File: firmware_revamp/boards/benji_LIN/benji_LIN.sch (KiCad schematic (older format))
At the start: 41 parts, among them J1 CONN_02X03, U1 MCP2561-E_SN, U101 TPS560430YF, U2 ATMEGA16M1, U3 TLIN1021DRQ1, Y1 Crystal_SMD

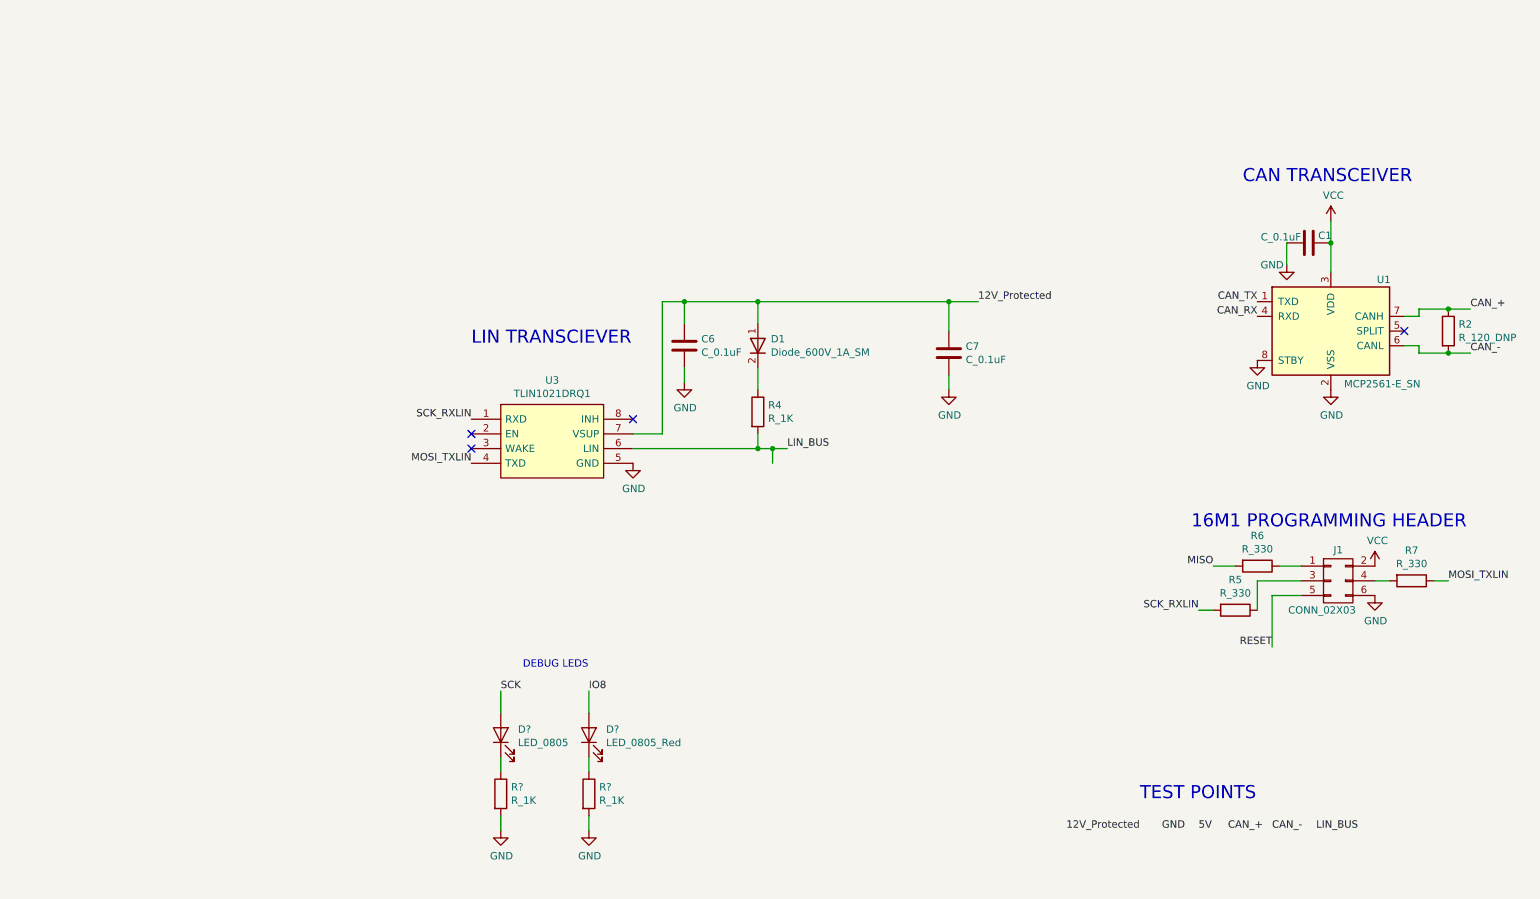
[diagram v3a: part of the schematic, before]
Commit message: Added blank headers, fixed programming resistors
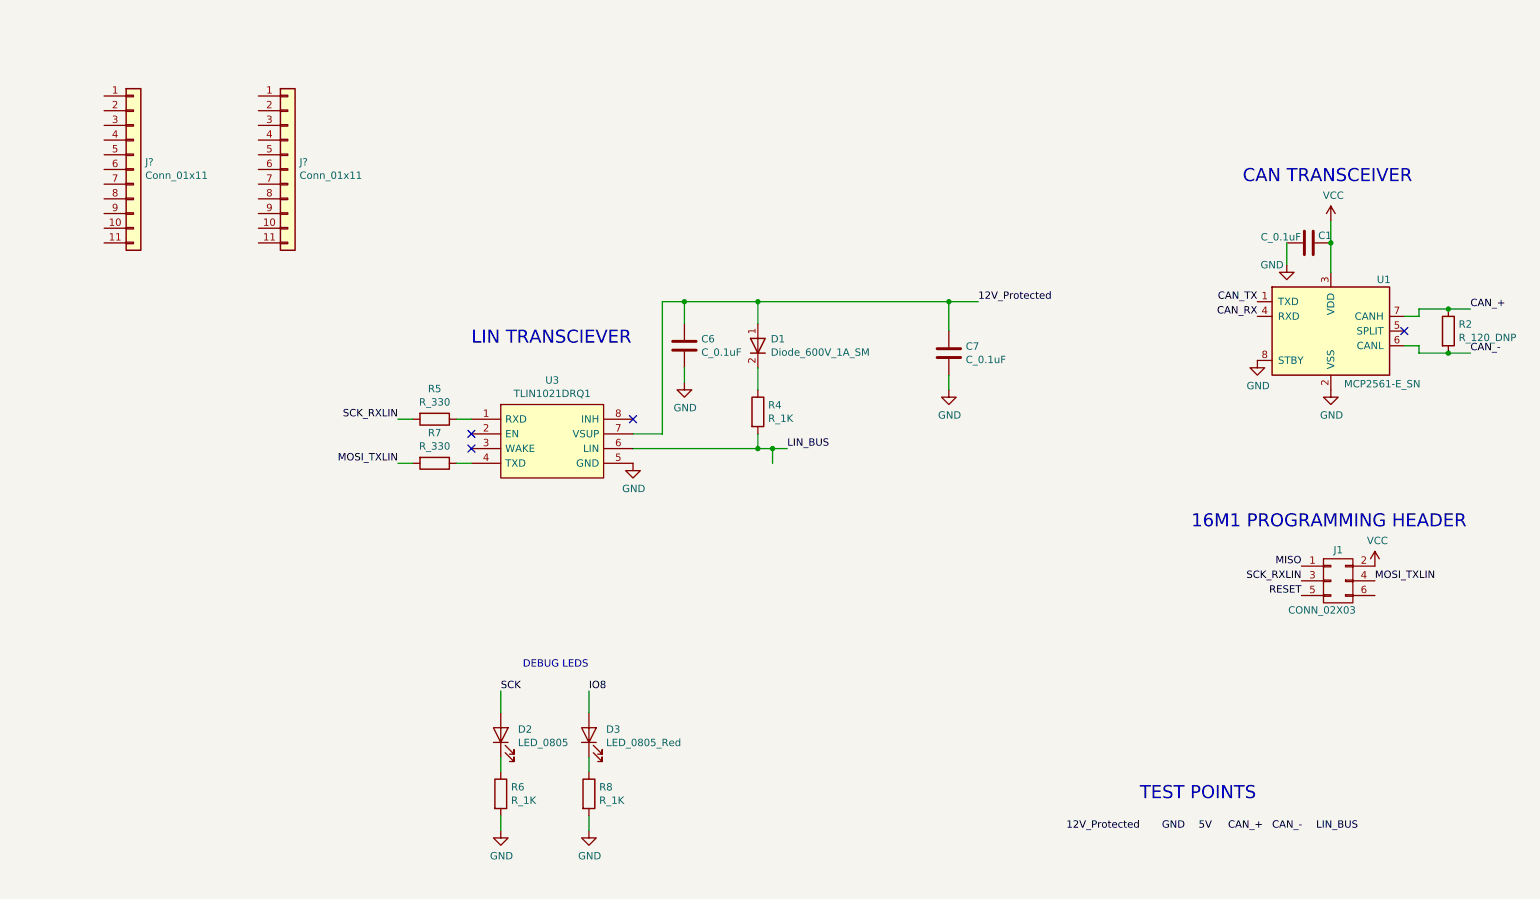
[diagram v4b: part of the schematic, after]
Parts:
- removed R6: R_330, footprints:R_0805_OEM, symbol formula:R_330
- added J? (x2): Conn_01x11, footprints:PinHeader_1x11_P2.54mm_Vertical, symbol formula:Conn_01x11
- gave numbers to parts that had none: 4
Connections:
- net GND: no longer J1.6 (P6)
- net MISO: now also J1.1 (P1)
- net MOSI_TXLIN: now also J1.4 (P4), R7.2; no longer R7.1, U3.4 (TXD)
- net SCK_RXLIN: now also J1.3 (P3); no longer U3.1 (RXD)
- net at R5.1: now also U3.1 (RXD); no longer J1.3 (P3)
- new net: R7.1, U3.4 (TXD)
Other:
- moved on the sheet: R7
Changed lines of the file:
@@
 Text Label 13300 7500 2    50   ~ 0
 GND
-Text Label 14600 4500 0    50   ~ 0
+Text Label 14100 4500 0    50   ~ 0
 MOSI_TXLIN
-$Comp
-L power:GND #PWR09
-U 1 1 5D62962D
-P 14100 4600
-F 0 "#PWR09" H 14100 4350 50  0001 C CNN
-F 1 "GND" H 14105 4427 50  0000 C CNN
-F 2 "" H 14100 4600 50  0001 C CNN
-F 3 "" H 14100 4600 50  0001 C CNN
-	1    14100 4600
-	1    0    0    -1
-$EndComp
 $Comp
 L power:VCC #PWR07
@@
 Text Label 3650 3100 0    50   ~ 0
 MOSI_TXLIN
-Text Label 7950 3400 2    50   ~ 0
+Text Label 7450 3400 2    50   ~ 0
 SCK_RXLIN
-Text Label 7950 3700 2    50   ~ 0
+Text Label 7450 3700 2    50   ~ 0
 MOSI_TXLIN
 $Comp
@@
 Wire Wire Line
 	2250 7350 2600 7350
-Text Label 12900 4700 2    50   ~ 0
+Text Label 13600 4500 2    50   ~ 0
 SCK_RXLIN
 $Comp
@@
 	1    0    0    -1
 $EndComp
-Text Label 13000 4400 2    50   ~ 0
+Text Label 13600 4400 2    50   ~ 0
 MISO
-Text Label 13400 4950 2    50   ~ 0
+Text Label 13600 4600 2    50   ~ 0
 RESET
 $Comp
 L formula:R_330 R7
 U 1 1 602CA042
-P 14350 4500
-F 0 "R7" V 14143 4500 50  0000 C CNN
-F 1 "R_330" V 14234 4500 50  0000 C CNN
-F 2 "footprints:R_0805_OEM" H 14280 4500 50  0001 C CNN
-F 3 "https://www.seielect.com/Catalog/SEI-RMCF_RMCP.pdf" H 14430 4500 50  0001 C CNN
-F 4 "DK" H 14350 4500 60  0001 C CNN "MFN"
-F 5 "RMCF0805FT330RCT-ND" H 14350 4500 60  0001 C CNN "MPN"
-F 6 "https://www.digikey.com/product-detail/en/stackpole-electronics-inc/RMCF0805FT330R/RMCF0805FT330RCT-ND/1942351" H 14830 4900 60  0001 C CNN "PurchasingLink"
-	1    14350 4500
+P 7700 3700
+F 0 "R7" V 7493 3700 50  0000 C CNN
+F 1 "R_330" V 7584 3700 50  0000 C CNN
+F 2 "footprints:R_0805_OEM" H 7630 3700 50  0001 C CNN
+F 3 "https://www.seielect.com/Catalog/SEI-RMCF_RMCP.pdf" H 7780 3700 50  0001 C CNN
+F 4 "DK" H 7700 3700 60  0001 C CNN "MFN"
+F 5 "RMCF0805FT330RCT-ND" H 7700 3700 60  0001 C CNN "MPN"
+F 6 "https://www.digikey.com/product-detail/en/stackpole-electronics-inc/RMCF0805FT330R/RMCF0805FT330RCT-ND/1942351" H 8180 4100 60  0001 C CNN "PurchasingLink"
+	1    7700 3700
 	0    1    1    0
 $EndComp
-Wire Wire Line
-	14100 4500 14200 4500
-Wire Wire Line
-	14500 4500 14600 4500
-$Comp
-L formula:R_330 R6
-U 1 1 602D41EE
-P 13300 4400
-F 0 "R6" V 13093 4400 50  0000 C CNN
-F 1 "R_330" V 13184 4400 50  0000 C CNN
-F 2 "footprints:R_0805_OEM" H 13230 4400 50  0001 C CNN
-F 3 "https://www.seielect.com/Catalog/SEI-RMCF_RMCP.pdf" H 13380 4400 50  0001 C CNN
-F 4 "DK" H 13300 4400 60  0001 C CNN "MFN"
-F 5 "RMCF0805FT330RCT-ND" H 13300 4400 60  0001 C CNN "MPN"
-F 6 "https://www.digikey.com/product-detail/en/stackpole-electronics-inc/RMCF0805FT330R/RMCF0805FT330RCT-ND/1942351" H 13780 4800 60  0001 C CNN "PurchasingLink"
-	1    13300 4400
-	0    1    1    0
-$EndComp
-Wire Wire Line
-	13150 4400 13000 4400
-Wire Wire Line
-	13450 4400 13600 4400
-Wire Wire Line
-	13400 4600 13600 4600
-$Comp
-L formula:R_330 R5
-U 1 1 602DEDF9
-P 13150 4700
-F 0 "R5" V 12943 4700 50  0000 C CNN
-F 1 "R_330" V 13034 4700 50  0000 C CNN
-F 2 "footprints:R_0805_OEM" H 13080 4700 50  0001 C CNN
-F 3 "https://www.seielect.com/Catalog/SEI-RMCF_RMCP.pdf" H 13230 4700 50  0001 C CNN
-F 4 "DK" H 13150 4700 60  0001 C CNN "MFN"
-F 5 "RMCF0805FT330RCT-ND" H 13150 4700 60  0001 C CNN "MPN"
-F 6 "https://www.digikey.com/product-detail/en/stackpole-electronics-inc/RMCF0805FT330R/RMCF0805FT330RCT-ND/1942351" H 13630 5100 60  0001 C CNN "PurchasingLink"
-	1    13150 4700
-	0    1    1    0
-$EndComp
-Wire Wire Line
-	13300 4700 13300 4500
-Wire Wire Line
-	13300 4500 13600 4500
-Wire Wire Line
-	13000 4700 12900 4700
-Wire Wire Line
-	13400 4600 13400 4950
 Text Label 2250 7050 0    50   ~ 0
 12V_Protected
@@
 IO8
 $Comp
-L formula:LED_0805 D?
+L formula:LED_0805 D2
 U 1 1 60323BBE
 P 8150 5550
-F 0 "D?" V 8189 5433 50  0000 R CNN
+F 0 "D2" V 8189 5433 50  0000 R CNN
 F 1 "LED_0805" V 8098 5433 50  0000 R CNN
 F 2 "footprints:LED_0805_OEM" H 8050 5550 50  0001 C CNN
@@
 	8150 5400 8150 5250
 $Comp
-L formula:LED_0805_Red D?
+L formula:LED_0805_Red D3
 U 1 1 60327C95
 P 8750 5550
-F 0 "D?" V 8789 5433 50  0000 R CNN
+F 0 "D3" V 8789 5433 50  0000 R CNN
 F 1 "LED_0805_Red" V 8698 5433 50  0000 R CNN
 F 2 "footprints:LED_0805_OEM" H 8650 5550 50  0001 C CNN
@@
 	8750 5250 8750 5400
 $Comp
-L formula:R_1K R?
+L formula:R_1K R6
 U 1 1 6032BF02
 P 8150 5950
-F 0 "R?" H 8220 5996 50  0000 L CNN
+F 0 "R6" H 8220 5996 50  0000 L CNN
 F 1 "R_1K" H 8220 5905 50  0000 L CNN
 F 2 "footprints:R_0805_OEM" H 8080 5950 50  0001 C CNN
@@
 $EndComp
 $Comp
-L formula:R_1K R?
+L formula:R_1K R8
 U 1 1 6032C9E2
 P 8750 5950
-F 0 "R?" H 8820 5996 50  0000 L CNN
+F 0 "R8" H 8820 5996 50  0000 L CNN
 F 1 "R_1K" H 8820 5905 50  0000 L CNN
 F 2 "footprints:R_0805_OEM" H 8680 5950 50  0001 C CNN
@@
 	8750 5700 8750 5800
 $Comp
-L power:GND #PWR?
+L power:GND #PWR09
 U 1 1 60332FFA
 P 8150 6200
-F 0 "#PWR?" H 8150 5950 50  0001 C CNN
+F 0 "#PWR09" H 8150 5950 50  0001 C CNN
 F 1 "GND" H 8155 6027 50  0000 C CNN
 F 2 "" H 8150 6200 50  0001 C CNN
@@
 	8150 6200 8150 6100
 $Comp
-L power:GND #PWR?
+L power:GND #PWR019
 U 1 1 6033649C
 P 8750 6200
-F 0 "#PWR?" H 8750 5950 50  0001 C CNN
+F 0 "#PWR019" H 8750 5950 50  0001 C CNN
 F 1 "GND" H 8755 6027 50  0000 C CNN
 F 2 "" H 8750 6200 50  0001 C CNN
@@
 Wire Wire Line
 	8750 6200 8750 6100
+$Comp
+L formula:R_330 R5
+U 1 1 603ADA0E
+P 7700 3400
+F 0 "R5" V 7493 3400 50  0000 C CNN
+F 1 "R_330" V 7584 3400 50  0000 C CNN
+F 2 "footprints:R_0805_OEM" H 7630 3400 50  0001 C CNN
+F 3 "https://www.seielect.com/Catalog/SEI-RMCF_RMCP.pdf" H 7780 3400 50  0001 C CNN
+F 4 "DK" H 7700 3400 60  0001 C CNN "MFN"
+F 5 "RMCF0805FT330RCT-ND" H 7700 3400 60  0001 C CNN "MPN"
+F 6 "https://www.digikey.com/product-detail/en/stackpole-electronics-inc/RMCF0805FT330R/RMCF0805FT330RCT-ND/1942351" H 8180 3800 60  0001 C CNN "PurchasingLink"
+	1    7700 3400
+	0    1    1    0
+$EndComp
+Wire Wire Line
+	7450 3400 7550 3400
+Wire Wire Line
+	7850 3400 7950 3400
+Wire Wire Line
+	7450 3700 7550 3700
+Wire Wire Line
+	7850 3700 7950 3700
+$Comp
+L formula:Conn_01x11 J?
+U 1 1 603F6805
+P 5650 1750
+F 0 "J?" H 5730 1850 50  0000 L CNN
+F 1 "Conn_01x11" H 5730 1759 50  0000 L CNN
+F 2 "footprints:PinHeader_1x11_P2.54mm_Vertical" H 5550 2450 50  0001 C CNN
+F 3 "" H 5650 1750 50  0001 C CNN
+	1    5650 1750
+	1    0    0    -1
+$EndComp
+$Comp
+L formula:Conn_01x11 J?
+U 1 1 6040C0B1
+P 6700 1750
+F 0 "J?" H 6780 1850 50  0000 L CNN
+F 1 "Conn_01x11" H 6780 1759 50  0000 L CNN
+F 2 "footprints:PinHeader_1x11_P2.54mm_Vertical" H 6600 2450 50  0001 C CNN
+F 3 "" H 6700 1750 50  0001 C CNN
+	1    6700 1750
+	1    0    0    -1
+$EndComp
 $EndSCHEMATC

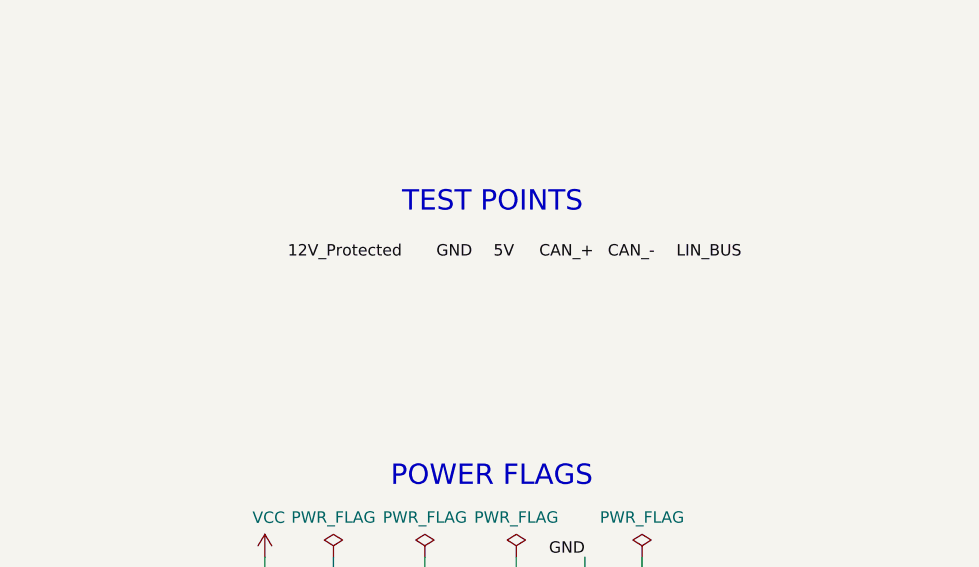
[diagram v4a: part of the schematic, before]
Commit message: Add test point parts
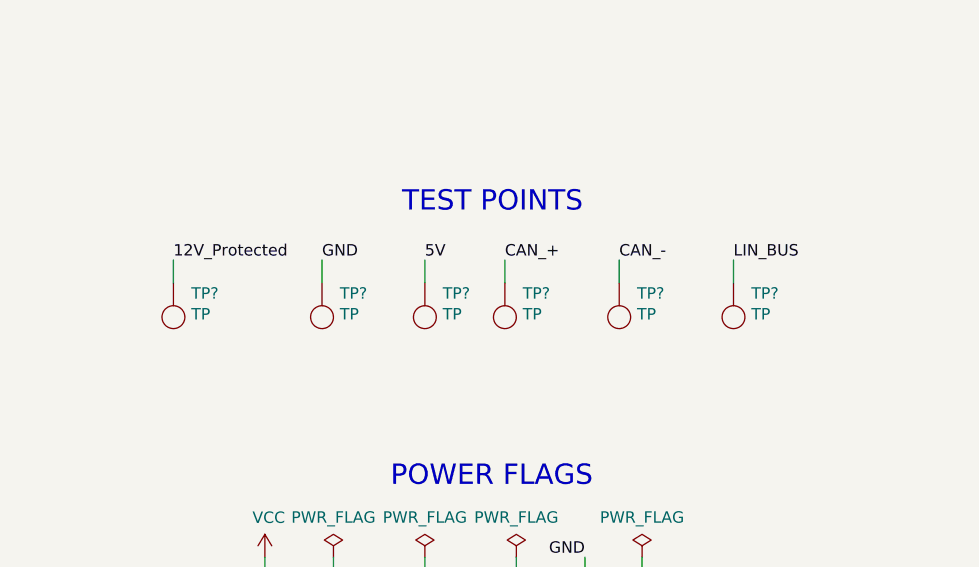
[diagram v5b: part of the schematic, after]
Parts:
- added TP? (x6): TP, footprints:tp_1.6mm, symbol formula:TP
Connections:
- net 12V_Protected: now also TP?.1 (TP)
- net CAN_+: now also TP?.1 (TP)
- net CAN_-: now also TP?.1 (TP)
- net GND: now also TP?.1 (TP)
- net LIN_BUS: now also TP?.1 (TP)
- net VCC: now also TP?.1 (TP)
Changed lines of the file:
@@
 Wire Wire Line
 	13550 7500 13550 7650
-Text Notes 12500 6000 0    89   ~ 0
-TEST POINTS
-Text Label 12000 6200 0    50   ~ 0
-12V_Protected
-Text Label 12650 6200 0    50   ~ 0
+Text Label 12150 6200 0    50   ~ 0
 GND
-Text Label 12900 6200 0    50   ~ 0
+Text Label 12600 6200 0    50   ~ 0
 5V
-Text Label 13100 6200 0    50   ~ 0
+Text Label 12950 6200 0    50   ~ 0
 CAN_+
-Text Label 13400 6200 0    50   ~ 0
+Text Label 13450 6200 0    50   ~ 0
 CAN_-
-Text Label 13700 6200 0    50   ~ 0
+Text Label 13950 6200 0    50   ~ 0
 LIN_BUS
 Text Notes 8300 5100 0    50   ~ 0
@@
 	1    0    0    -1
 $EndComp
+$Comp
+L formula:TP TP?
+U 1 1 6043188E
+P 12150 6500
+F 0 "TP?" H 12072 6346 50  0000 R CNN
+F 1 "TP" H 12072 6437 50  0000 R CNN
+F 2 "footprints:tp_1.6mm" H 12050 6400 50  0001 C CNN
+F 3 "http://www.keyelco.com/product-pdf.cfm?p=1314" H 12150 6500 50  0001 C CNN
+F 4 "DK" H 12250 6600 50  0001 C CNN "MFN"
+F 5 "36-5006-ND" H 12350 6700 50  0001 C CNN "MPN"
+F 6 "https://www.digikey.com/product-detail/en/keystone-electronics/5006/36-5006-ND/255330" H 12450 6800 50  0001 C CNN "PurchasingLink"
+	1    12150 6500
+	-1   0    0    1
+$EndComp
+$Comp
+L formula:TP TP?
+U 1 1 60452016
+P 12600 6500
+F 0 "TP?" H 12522 6346 50  0000 R CNN
+F 1 "TP" H 12522 6437 50  0000 R CNN
+F 2 "footprints:tp_1.6mm" H 12500 6400 50  0001 C CNN
+F 3 "http://www.keyelco.com/product-pdf.cfm?p=1314" H 12600 6500 50  0001 C CNN
+F 4 "DK" H 12700 6600 50  0001 C CNN "MFN"
+F 5 "36-5006-ND" H 12800 6700 50  0001 C CNN "MPN"
+F 6 "https://www.digikey.com/product-detail/en/keystone-electronics/5006/36-5006-ND/255330" H 12900 6800 50  0001 C CNN "PurchasingLink"
+	1    12600 6500
+	-1   0    0    1
+$EndComp
+$Comp
+L formula:TP TP?
+U 1 1 60452657
+P 12950 6500
+F 0 "TP?" H 12872 6346 50  0000 R CNN
+F 1 "TP" H 12872 6437 50  0000 R CNN
+F 2 "footprints:tp_1.6mm" H 12850 6400 50  0001 C CNN
+F 3 "http://www.keyelco.com/product-pdf.cfm?p=1314" H 12950 6500 50  0001 C CNN
+F 4 "DK" H 13050 6600 50  0001 C CNN "MFN"
+F 5 "36-5006-ND" H 13150 6700 50  0001 C CNN "MPN"
+F 6 "https://www.digikey.com/product-detail/en/keystone-electronics/5006/36-5006-ND/255330" H 13250 6800 50  0001 C CNN "PurchasingLink"
+	1    12950 6500
+	-1   0    0    1
+$EndComp
+$Comp
+L formula:TP TP?
+U 1 1 60452C4A
+P 13450 6500
+F 0 "TP?" H 13372 6346 50  0000 R CNN
+F 1 "TP" H 13372 6437 50  0000 R CNN
+F 2 "footprints:tp_1.6mm" H 13350 6400 50  0001 C CNN
+F 3 "http://www.keyelco.com/product-pdf.cfm?p=1314" H 13450 6500 50  0001 C CNN
+F 4 "DK" H 13550 6600 50  0001 C CNN "MFN"
+F 5 "36-5006-ND" H 13650 6700 50  0001 C CNN "MPN"
+F 6 "https://www.digikey.com/product-detail/en/keystone-electronics/5006/36-5006-ND/255330" H 13750 6800 50  0001 C CNN "PurchasingLink"
+	1    13450 6500
+	-1   0    0    1
+$EndComp
+$Comp
+L formula:TP TP?
+U 1 1 604534CE
+P 13950 6500
+F 0 "TP?" H 13872 6346 50  0000 R CNN
+F 1 "TP" H 13872 6437 50  0000 R CNN
+F 2 "footprints:tp_1.6mm" H 13850 6400 50  0001 C CNN
+F 3 "http://www.keyelco.com/product-pdf.cfm?p=1314" H 13950 6500 50  0001 C CNN
+F 4 "DK" H 14050 6600 50  0001 C CNN "MFN"
+F 5 "36-5006-ND" H 14150 6700 50  0001 C CNN "MPN"
+F 6 "https://www.digikey.com/product-detail/en/keystone-electronics/5006/36-5006-ND/255330" H 14250 6800 50  0001 C CNN "PurchasingLink"
+	1    13950 6500
+	-1   0    0    1
+$EndComp
+Wire Wire Line
+	12150 6300 12150 6200
+Wire Wire Line
+	12600 6200 12600 6300
+Wire Wire Line
+	12950 6300 12950 6200
+Wire Wire Line
+	13450 6200 13450 6300
+Wire Wire Line
+	13950 6300 13950 6200
+Text Notes 12500 6000 0    89   ~ 0
+TEST POINTS
+Wire Wire Line
+	11500 6200 11500 6300
+$Comp
+L formula:TP TP?
+U 1 1 6042FA03
+P 11500 6500
+F 0 "TP?" H 11422 6346 50  0000 R CNN
+F 1 "TP" H 11422 6437 50  0000 R CNN
+F 2 "footprints:tp_1.6mm" H 11400 6400 50  0001 C CNN
+F 3 "http://www.keyelco.com/product-pdf.cfm?p=1314" H 11500 6500 50  0001 C CNN
+F 4 "DK" H 11600 6600 50  0001 C CNN "MFN"
+F 5 "36-5006-ND" H 11700 6700 50  0001 C CNN "MPN"
+F 6 "https://www.digikey.com/product-detail/en/keystone-electronics/5006/36-5006-ND/255330" H 11800 6800 50  0001 C CNN "PurchasingLink"
+	1    11500 6500
+	-1   0    0    1
+$EndComp
+Text Label 11500 6200 0    50   ~ 0
+12V_Protected
 $EndSCHEMATC
